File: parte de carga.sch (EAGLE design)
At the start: 33 parts, among them IC1 MCP73831T-2ACI_OT, IC10 741G3157DBVR, IC15 LMV321AIDCKR, IC16 LMV321AIDCKR, IC2 ESP32-S3-WROOM-1-N16R8, IC5 LMV321AIDCKR, IC7 AD8226ARZ, IC9 LP38692MP-3.3_NOPB, J1 USB3500-30-A-KIT

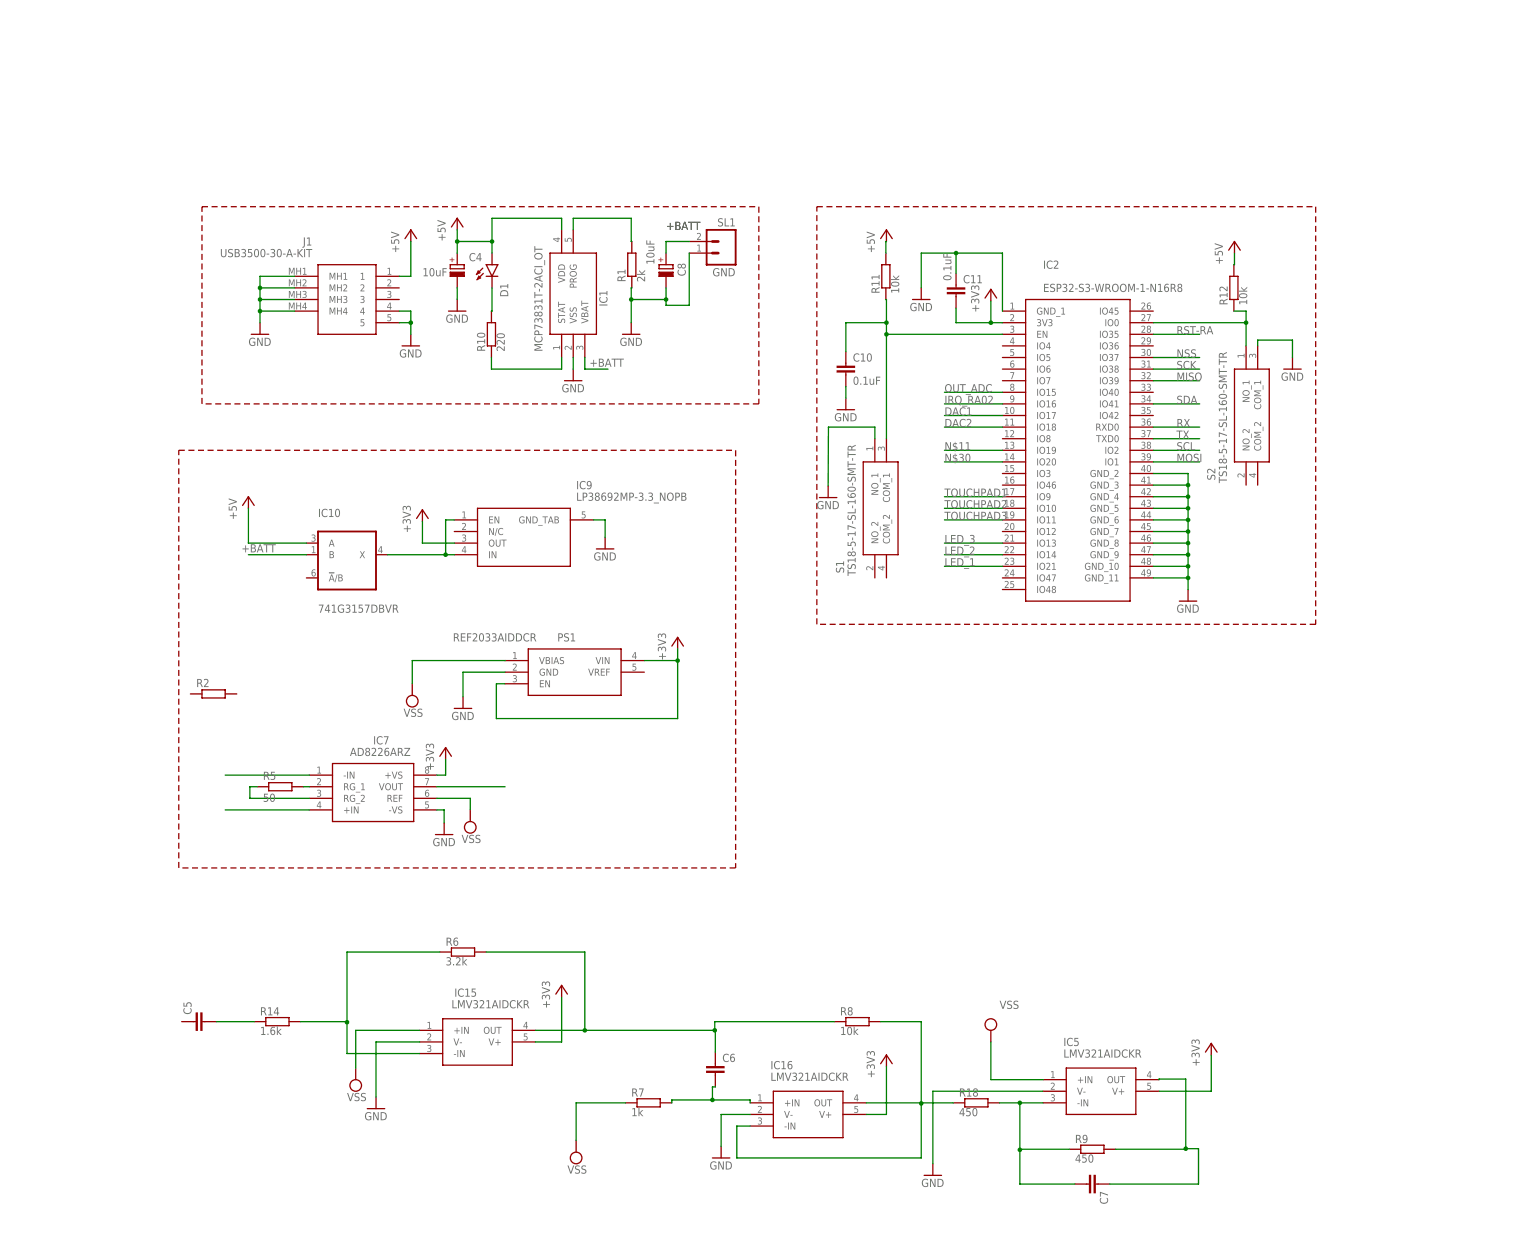
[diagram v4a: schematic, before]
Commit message: arregle las resistencias, condensadores y diodo
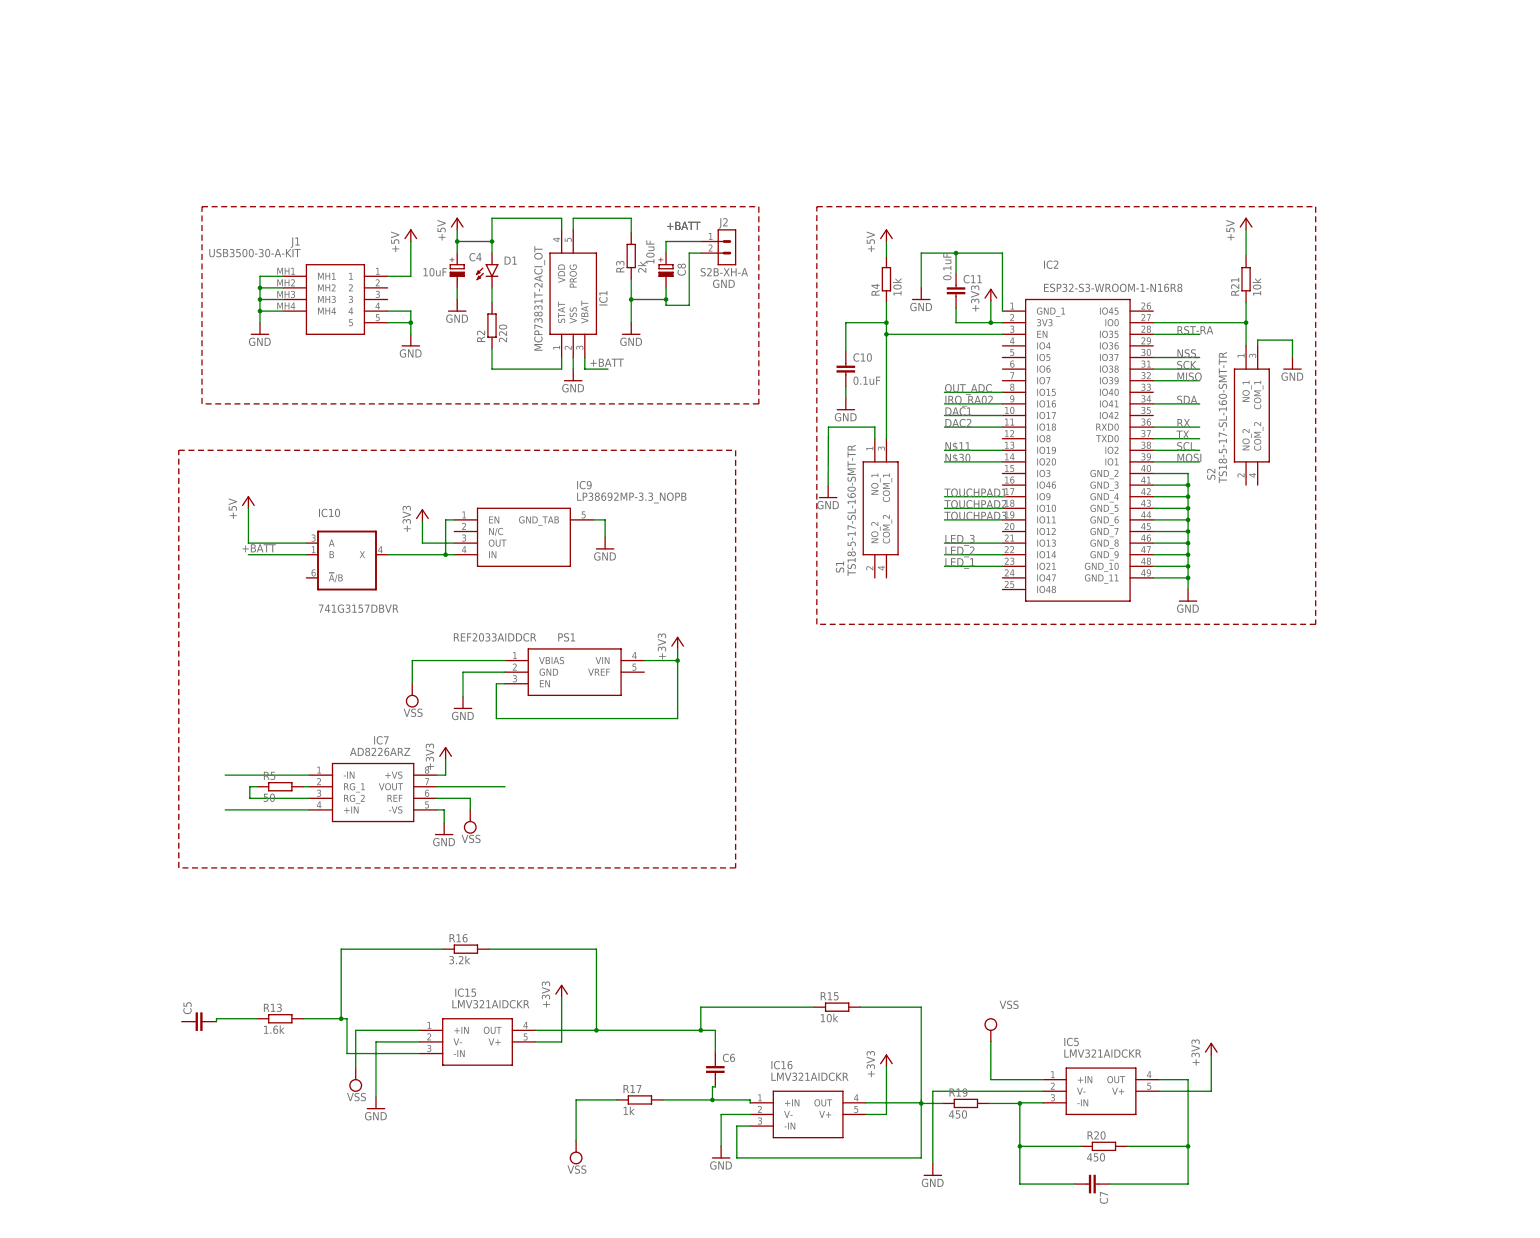
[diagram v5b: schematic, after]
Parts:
- removed R1: 2k, resistor-shunt:BVS
- removed R10: 220, resistor-shunt:BVS
- removed R11, R12, R8: 10k, resistor-shunt:BVS
- removed R14: 1.6k, resistor-shunt:BVS
- removed R18, R9: 450, resistor-shunt:BVS
- removed R6: 3.2k, resistor-shunt:BVS
- removed R7: 1k, resistor-shunt:BVS
- removed SL1: (no value), con-amp-quick:M02
- added J2: S2B-XH-A, Connector:S2B-XH-A
- added R13: 1.6k, rcl:R-EU_R0805
- added R15, R21, R4: 10k, rcl:R-EU_R0805
- added R16: 3.2k, rcl:R-EU_R0805
- added R17: 1k, rcl:R-EU_R0805
- added R19, R20: 450, rcl:R-EU_R0805
- added R3: 2k, rcl:R-EU_R0805
- C10, C11, C5, C6, C7: device capacitor-wima:C2.5/6 -> capacitor-wima:C2.5/5
- D1: value SFH482 -> CHIP-FLAT-G_0603-0.35MM; device led:SFH482 -> LED:CHIP-FLAT-G_0603-0.35MM; C3 10U -> (none)
- R2: value (none) -> 220
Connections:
- removed net N$7: C7.1, IC5.OUT, R9.1
- new net N$14: C5.2, R13.1
- net +5V: now also R21.2, R4.2; no longer R11.1, R12.1
- net +BATT: now also J2.1; no longer SL1.2
- net GND: now also J2.2, R3.1; no longer R1.2, SL1.1
- net N$1: now also R2.2; no longer R10.1
- net N$13: now also R17.2; no longer R7.1
- net N$2: now also R2.1; no longer R10.2
- net N$3: now also R3.2; no longer R1.1
- net N$4: now also R4.1; no longer R11.2
- net N$46: now also R13.2, R16.1; no longer R14.1, R6.2
- net N$47: now also R15.1, R16.2; no longer R6.1, R8.2
- net N$5: now also R21.1; no longer R12.2
- net N$6: now also IC16.-IN, IC16.OUT, R15.2, R19.1; no longer C5.2, R14.2
- net N$8: now also C7.1, IC5.OUT, R20.2; no longer IC16.-IN, IC16.OUT, R18.2, R8.1
- net N$9: now also R19.2, R20.1; no longer R18.1, R9.2
- net VSS: now also R17.1; no longer R7.2
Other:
- moved on the sheet: J1, R2

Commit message: areglé parte del puerto usb, y el conector de elctrodos, saqué un conector de 3 pines rx. tx, gnd. saqué un conector para el display
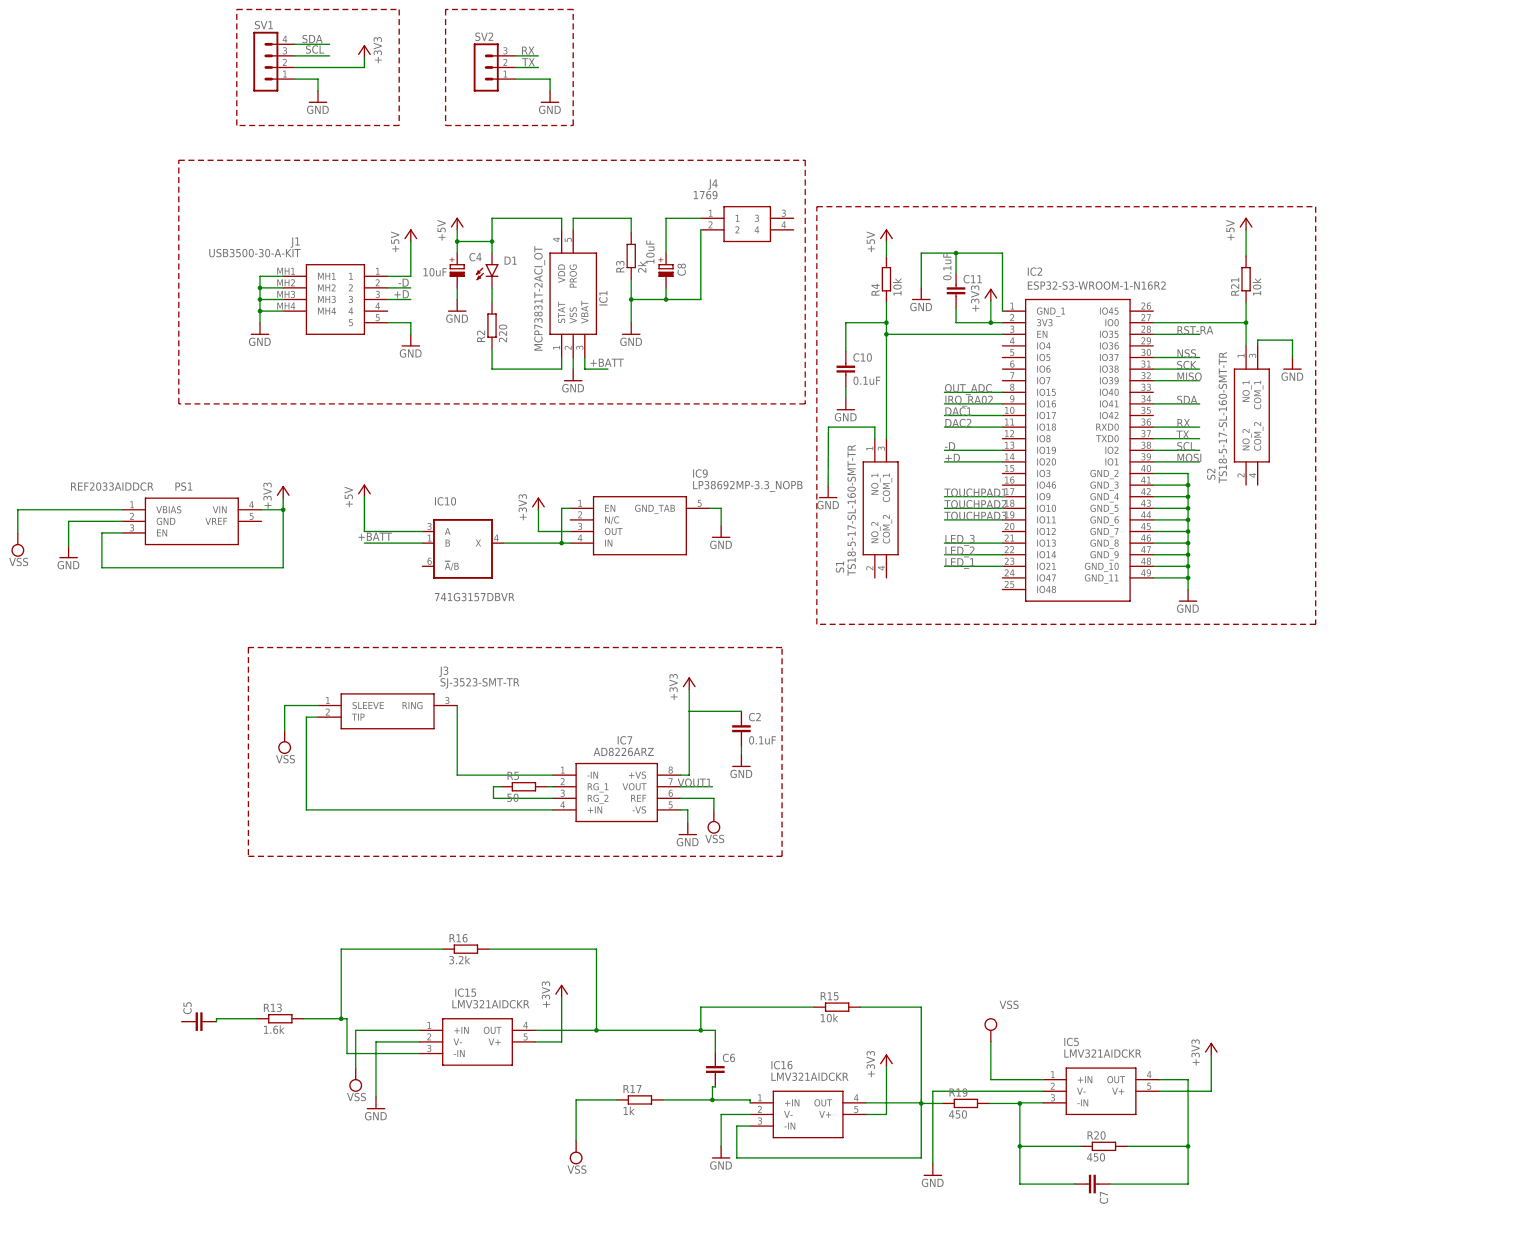
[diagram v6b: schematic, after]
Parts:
- removed J2: S2B-XH-A, Connector:S2B-XH-A
- added C2: 0.1uF, capacitor-wima:C2.5/5
- added J3: SJ-3523-SMT-TR, SJ-3523-SMT-TR:SJ-3523-SMT-TR
- added J4: 1769, 1769:1769
- added SV1: (no value), con-lstb:MA04-1
- added SV2: (no value), con-lstb:MA03-1
- IC2: value ESP32-S3-WROOM-1-N16R8 -> ESP32-S3-WROOM-1-N16R2; device ESP32-S3-WROOM-1-N16R8:ESP32-S3-WROOM-1-N16R8 -> ESP32-S3-WROOM-1-N16R2:ESP32-S3-WROOM-1-N16R2
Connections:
- net N$19 renamed VOUT1
- removed net N$20: IC7.+IN
- removed net N$30: IC2.IO20
- new net +D: IC2.IO20, J1.3
- new net -D: IC2.IO19, J1.2
- new net N$19: C8.+, J4.1
- net +3V3: now also C2.1, SV1.2
- net +BATT: no longer C8.+, J2.1
- net GND: now also C2.2, J4.2, SV1.1, SV2.1; no longer J1.4, J2.2
- net N$11: now also IC7.-IN, J3.RING; no longer IC2.IO19
- net N$17: now also IC7.+IN, J3.TIP; no longer IC7.-IN
- net RX: now also SV2.3
- net SCL: now also SV1.3
- net SDA: now also SV1.4
- net TX: now also SV2.2
- net VSS: now also J3.SLEEVE
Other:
- moved on the sheet: IC10, IC7, IC9, PS1, R5

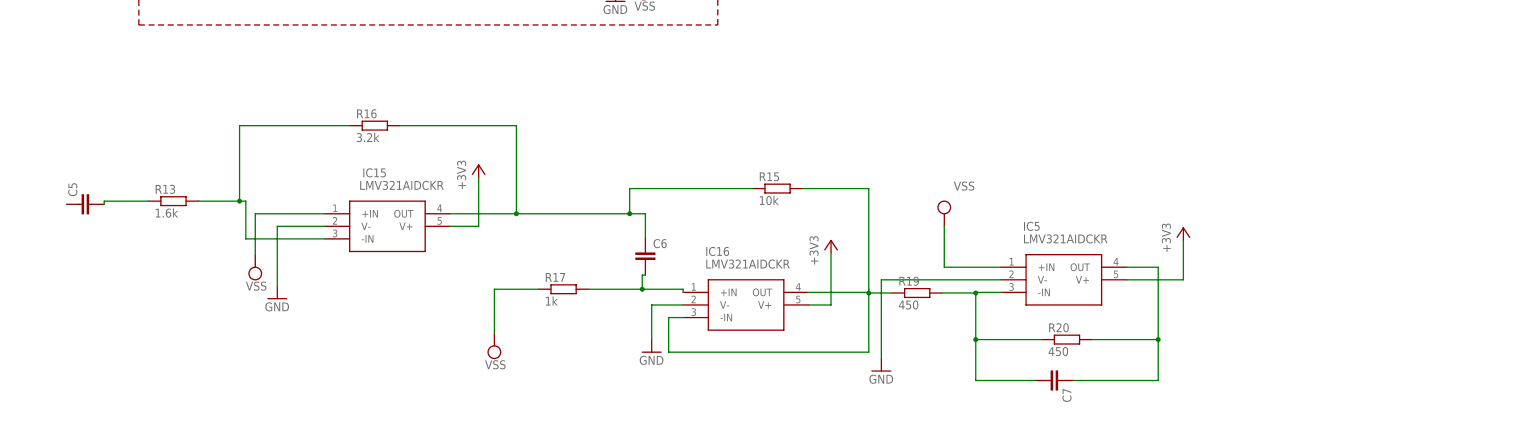
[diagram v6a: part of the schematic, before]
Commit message: Corregir huellas capacitores, organice esp32 y Amp Op
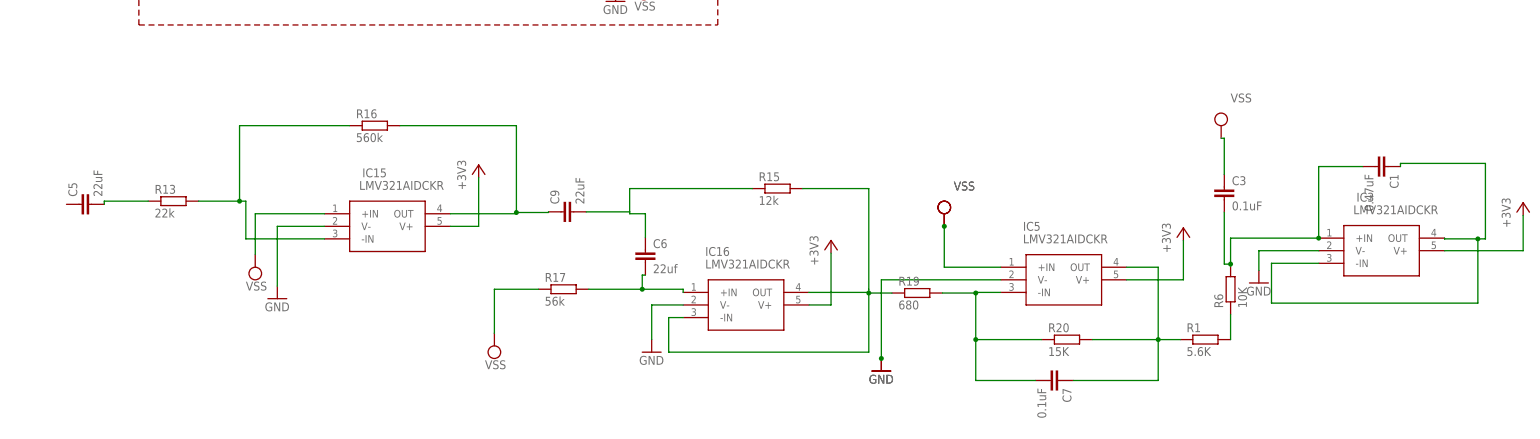
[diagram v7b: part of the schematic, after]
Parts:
- added C1: 0.47uF, capacitor-wima:C2.5/5
- added C3: 0.1uF, capacitor-wima:C2.5/5
- added C9: 22uF, capacitor-wima:C2.5/5
- added IC3: LMV321AIDCKR, LMV321AIDCKR:LMV321AIDCKR
- added R1: 5.6K, rcl:R-EU_R0805
- added R6: 10K, rcl:R-EU_R0805
- C5: value (none) -> 22uF; POPULARITY (none) -> 22uf
- C6: value (none) -> 22uf
- C7: value (none) -> 0.1uF
- R13: value 1.6k -> 22k
- R15: value 10k -> 12k
- R16: value 3.2k -> 560k
- R17: value 1k -> 56k
- R19: value 450 -> 680
- R20: value 450 -> 15K
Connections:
- new net N$16: C1.1, IC3.-IN, IC3.OUT
- new net N$18: C6.1, C9.2, R15.1
- new net N$20: R1.2, R6.1
- new net N$7: C1.2, C3.2, IC3.+IN, R6.2
- net +3V3: now also IC3.V+
- net GND: now also IC3.V-
- net N$47: now also C9.1; no longer C6.1, R15.1
- net N$8: now also R1.1
- net VSS: now also C3.1

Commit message: Astudillo estuvo aqui
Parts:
- removed D1: CHIP-FLAT-G_0603-0.35MM, LED:CHIP-FLAT-G_0603-0.35MM
- added LED1: 599-0181-007F, 599-0181-007F:599-0181-007F
- C1, C10, C11, C2, C3, C6, C7: device capacitor-wima:C2.5/5 -> GCM21B5C2A393JE02L:GCM21B5C2A393JE02L
- C4, C8: device Capacitor:C-POL_TANTALUM-1206(3216-METRIC) -> GCM21B5C2A393JE02L:GCM21B5C2A393JE02L
- C5, C9: device capacitor-wima:C2.5/5 -> GCM21B5C2A393JE02L:GCM21B5C2A393JE02L; POPULARITY 22uf -> (none)
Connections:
- removed net N$1 (its old number): D1.C, R2.2
- new net N$2: LED1.K, R2.2
- net +5V: now also C8.1, LED1.A; no longer C4.+, D1.A
- net GND: now also C4.2, C8.2; no longer C4.-, C8.-
- net N$19: now also C4.1; no longer C8.+
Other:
- moved on the sheet: R2
